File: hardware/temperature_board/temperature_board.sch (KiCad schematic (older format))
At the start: 11 parts

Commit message: pollin eval board datasheet added
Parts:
- removed C?: 100nF, ~, symbol C
- removed C?: 330nF, ~, symbol C
- removed K?: CONN_3, ~, symbol CONN_3
- removed U?: LM7805, ~, symbol LM7805
- added C?: 100nF, ~, symbol C
- added R? (x2): 120, ~, symbol R
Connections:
- net labels removed: Vin
- wire segments 44 -> 33
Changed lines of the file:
@@
 LIBS:TSic50xF
 LIBS:ST485
+LIBS:temperature_board-cache
 EELAYER 27 0
 EELAYER END
@@
 Sheet 1 1
 Title ""
-Date "22 mar 2014"
+Date "11 apr 2014"
 Rev ""
 Comp ""
@@
 Comment4 ""
 $EndDescr
-$Comp
-L GND #PWR?
-U 1 1 532DBFDE
-P 5750 6000
-F 0 "#PWR?" H 5750 6000 30  0001 C CNN
-F 1 "GND" H 5750 5930 30  0001 C CNN
-F 2 "" H 5750 6000 60  0000 C CNN
-F 3 "" H 5750 6000 60  0000 C CNN
-	1    5750 6000
-	1    0    0    -1
-$EndComp
 $Comp
 L VCC #PWR?
@@
 	7700 3050 7800 3050
 Wire Wire Line
-	7800 3050 7800 3250
-Wire Wire Line
-	7800 3250 8200 3250
-Wire Wire Line
-	8000 3250 8000 3150
+	7800 3050 7800 3650
 Wire Wire Line
 	7800 2750 7800 2550
@@
 $EndComp
 $Comp
-L LM7805 U?
-U 1 1 532DDDDB
-P 5750 5200
-F 0 "U?" H 5900 5004 60  0000 C CNN
-F 1 "LM7805" H 5750 5400 60  0000 C CNN
-F 2 "~" H 5750 5200 60  0000 C CNN
-F 3 "~" H 5750 5200 60  0000 C CNN
-	1    5750 5200
-	-1   0    0    -1
-$EndComp
-$Comp
 L GND #PWR?
 U 1 1 532DDE77
@@
 Wire Wire Line
 	8800 3250 8800 3500
-$Comp
-L CONN_3 K?
-U 1 1 532DDF17
-P 5750 4750
-F 0 "K?" V 5700 4750 50  0000 C CNN
-F 1 "CONN_3" V 5800 4750 40  0000 C CNN
-F 2 "~" H 5750 4750 60  0000 C CNN
-F 3 "~" H 5750 4750 60  0000 C CNN
-	1    5750 4750
-	0    1    1    0
-$EndComp
-Wire Wire Line
-	5850 4400 5850 4250
-Wire Wire Line
-	5850 4250 6350 4250
-Wire Wire Line
-	6350 4250 6350 5300
-Wire Wire Line
-	6350 5150 6150 5150
-Wire Wire Line
-	5650 4400 5650 4250
-Wire Wire Line
-	5650 4250 5150 4250
-Wire Wire Line
-	5150 4250 5150 5300
-Wire Wire Line
-	5150 5150 5350 5150
-Text Label 5900 4050 2    60   ~ 0
-Vin
-Wire Wire Line
-	5750 4400 5750 4050
-Wire Wire Line
-	5750 4050 5900 4050
-Text Label 8700 3150 0    60   ~ 0
-Vin
 Wire Wire Line
 	8700 3150 8900 3150
@@
 L VCC #PWR?
 U 1 1 532DE001
-P 4700 4150
-F 0 "#PWR?" H 4700 4250 30  0001 C CNN
-F 1 "VCC" H 4700 4250 30  0000 C CNN
-F 2 "" H 4700 4150 60  0000 C CNN
-F 3 "" H 4700 4150 60  0000 C CNN
-	1    4700 4150
-	1    0    0    -1
-$EndComp
-Wire Wire Line
-	5150 4700 4700 4700
-Wire Wire Line
-	4700 4700 4700 4150
-Connection ~ 5150 4700
-Wire Wire Line
-	5750 5450 5750 6000
+P 8700 3050
+F 0 "#PWR?" H 8700 3150 30  0001 C CNN
+F 1 "VCC" H 8700 3150 30  0000 C CNN
+F 2 "" H 8700 3050 60  0000 C CNN
+F 3 "" H 8700 3050 60  0000 C CNN
+	1    8700 3050
+	1    0    0    -1
+$EndComp
+Connection ~ 8000 2550
 $Comp
 L C C?
-U 1 1 532DE060
-P 5150 5500
-F 0 "C?" H 5150 5600 40  0000 L CNN
-F 1 "100nF" H 5156 5415 40  0000 L CNN
-F 2 "~" H 5188 5350 30  0000 C CNN
-F 3 "~" H 5150 5500 60  0000 C CNN
-	1    5150 5500
+U 1 1 534839D5
+P 8000 3450
+F 0 "C?" H 8000 3550 40  0000 L CNN
+F 1 "100nF" H 8006 3365 40  0000 L CNN
+F 2 "~" H 8038 3300 30  0000 C CNN
+F 3 "~" H 8000 3450 60  0000 C CNN
+	1    8000 3450
 	-1   0    0    1
 $EndComp
-$Comp
-L C C?
-U 1 1 532DE066
-P 6350 5500
-F 0 "C?" H 6350 5600 40  0000 L CNN
-F 1 "330nF" H 6356 5415 40  0000 L CNN
-F 2 "~" H 6388 5350 30  0000 C CNN
-F 3 "~" H 6350 5500 60  0000 C CNN
-	1    6350 5500
-	-1   0    0    1
-$EndComp
-Connection ~ 5150 5150
-Connection ~ 6350 5150
-Wire Wire Line
-	5150 5700 5150 5800
-Wire Wire Line
-	5150 5800 6350 5800
-Connection ~ 5750 5800
-Wire Wire Line
-	6350 5800 6350 5700
-Connection ~ 8000 2550
-Wire Wire Line
-	8900 2650 8200 2650
-Wire Wire Line
-	8200 2650 8200 3250
-Connection ~ 8000 3250
+Wire Wire Line
+	8000 3150 8000 3250
+Wire Wire Line
+	7800 3650 8200 3650
+Wire Wire Line
+	8200 3650 8200 2650
+Wire Wire Line
+	8200 2650 8900 2650
+Connection ~ 8000 3650
+$Comp
+L R R?
+U 1 1 53483A7B
+P 8300 1950
+F 0 "R?" V 8380 1950 40  0000 C CNN
+F 1 "120" V 8307 1951 40  0000 C CNN
+F 2 "~" V 8230 1950 30  0000 C CNN
+F 3 "~" H 8300 1950 30  0000 C CNN
+	1    8300 1950
+	1    0    0    -1
+$EndComp
+$Comp
+L R R?
+U 1 1 53483A81
+P 8450 3200
+F 0 "R?" V 8530 3200 40  0000 C CNN
+F 1 "120" V 8457 3201 40  0000 C CNN
+F 2 "~" V 8380 3200 30  0000 C CNN
+F 3 "~" H 8450 3200 30  0000 C CNN
+	1    8450 3200
+	1    0    0    -1
+$EndComp
+Wire Wire Line
+	8300 2200 8300 2650
+Connection ~ 8300 2650
+Wire Wire Line
+	8450 2950 8450 2550
+Connection ~ 8450 2550
+$Comp
+L GND #PWR?
+U 1 1 53483B09
+P 8450 3750
+F 0 "#PWR?" H 8450 3750 30  0001 C CNN
+F 1 "GND" H 8450 3680 30  0001 C CNN
+F 2 "" H 8450 3750 60  0000 C CNN
+F 3 "" H 8450 3750 60  0000 C CNN
+	1    8450 3750
+	1    0    0    -1
+$EndComp
+$Comp
+L VCC #PWR?
+U 1 1 53483B0F
+P 8300 1550
+F 0 "#PWR?" H 8300 1650 30  0001 C CNN
+F 1 "VCC" H 8300 1650 30  0000 C CNN
+F 2 "" H 8300 1550 60  0000 C CNN
+F 3 "" H 8300 1550 60  0000 C CNN
+	1    8300 1550
+	1    0    0    -1
+$EndComp
+Wire Wire Line
+	8300 1550 8300 1700
+Wire Wire Line
+	8450 3450 8450 3750
+Wire Wire Line
+	8700 3050 8700 3150
 $EndSCHEMATC

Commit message: hardware + bestellungen
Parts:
- R? (x2): value 120 -> 22k
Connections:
- wire segments 33 -> 34
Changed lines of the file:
@@
 Sheet 1 1
 Title ""
-Date "11 apr 2014"
+Date "12 apr 2014"
 Rev ""
 Comp ""
@@
 P 8300 1950
 F 0 "R?" V 8380 1950 40  0000 C CNN
-F 1 "120" V 8307 1951 40  0000 C CNN
+F 1 "22k" V 8307 1951 40  0000 C CNN
 F 2 "~" V 8230 1950 30  0000 C CNN
 F 3 "~" H 8300 1950 30  0000 C CNN
@@
 P 8450 3200
 F 0 "R?" V 8530 3200 40  0000 C CNN
-F 1 "120" V 8457 3201 40  0000 C CNN
+F 1 "22k" V 8457 3201 40  0000 C CNN
 F 2 "~" V 8380 3200 30  0000 C CNN
 F 3 "~" H 8450 3200 30  0000 C CNN
@@
 Wire Wire Line
 	8700 3050 8700 3150
+$Comp
+L GND #PWR?
+U 1 1 534937C6
+P 9700 3600
+F 0 "#PWR?" H 9700 3600 30  0001 C CNN
+F 1 "GND" H 9700 3530 30  0001 C CNN
+F 2 "" H 9700 3600 60  0000 C CNN
+F 3 "" H 9700 3600 60  0000 C CNN
+	1    9700 3600
+	1    0    0    -1
+$EndComp
+Wire Wire Line
+	9700 3450 9700 3600
 $EndSCHEMATC

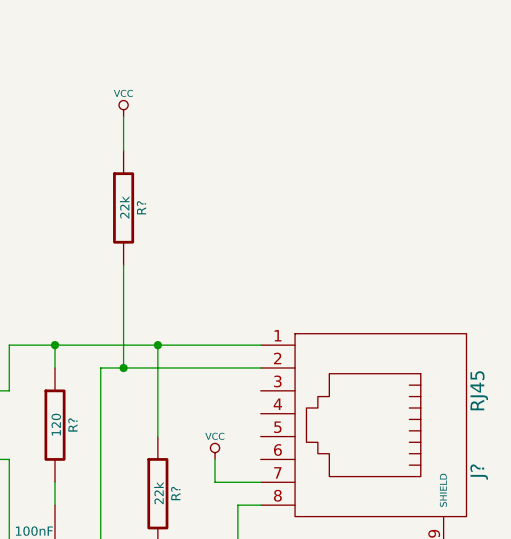
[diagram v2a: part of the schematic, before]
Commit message: comments in schematics
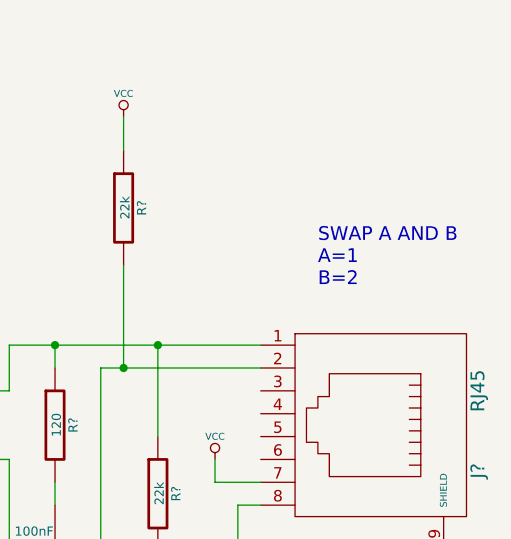
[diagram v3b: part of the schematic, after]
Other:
- note added: "SWAP A AND B\nA=1\nB=2"
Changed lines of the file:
@@
 Sheet 1 1
 Title ""
-Date "12 apr 2014"
+Date "28 apr 2014"
 Rev ""
 Comp ""
@@
 Wire Wire Line
 	9700 3450 9700 3600
+Text Notes 9150 2300 0    60   ~ 0
+SWAP A AND B\nA=1\nB=2
 $EndSCHEMATC
